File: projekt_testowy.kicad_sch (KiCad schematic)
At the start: 0 parts

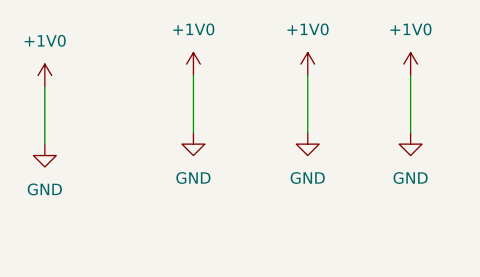
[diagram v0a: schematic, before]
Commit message: dodanie rezystorow na shemacie
4 rezystory tht
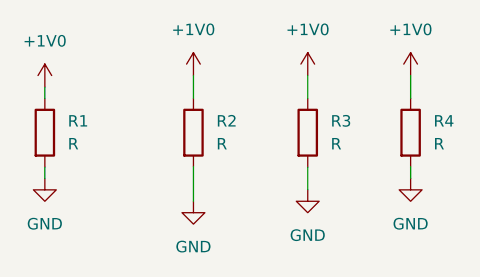
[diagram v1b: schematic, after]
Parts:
- added R1, R2, R3, R4: R, Resistor_THT:R_Axial_DIN0207_L6.3mm_D2.5mm_P10.16mm_Horizontal, symbol Device:R
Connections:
- net +1V0: now also R1.1, R2.1, R3.1, R4.1
- new net GND: R1.2, R2.2, R3.2, R4.2
